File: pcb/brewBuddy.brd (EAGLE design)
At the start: 45.7 x 86.4 mm, 3 parts

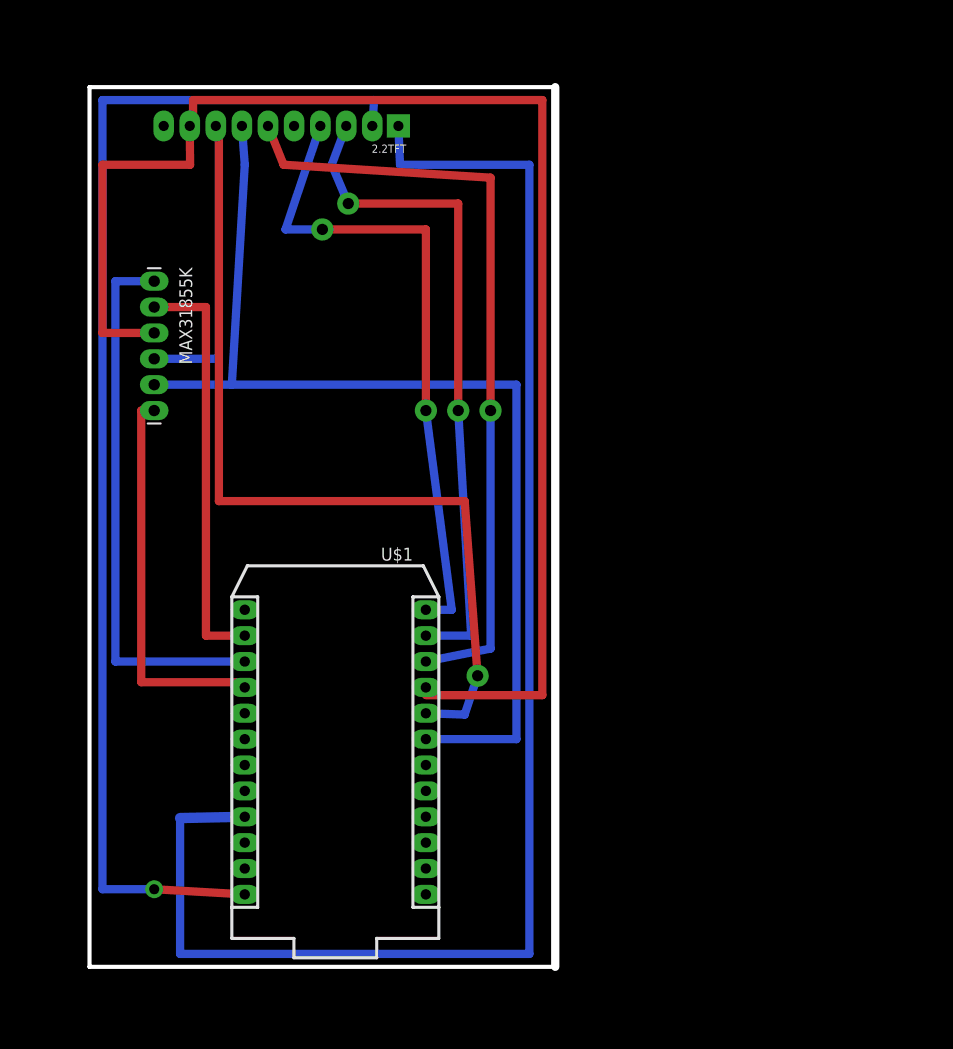
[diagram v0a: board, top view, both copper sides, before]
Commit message: updated brd for othermill
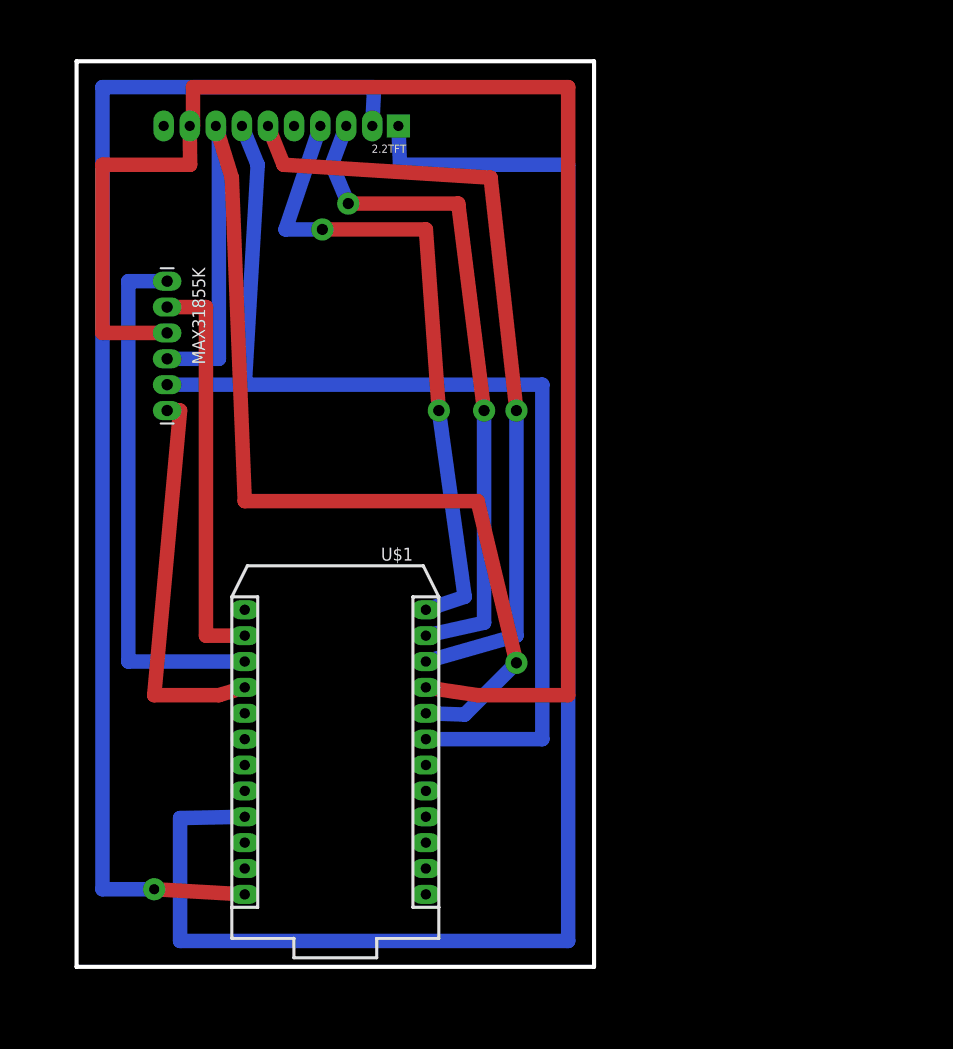
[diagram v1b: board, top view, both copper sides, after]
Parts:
- moved MAX31855K 1.27 mm to (7.62, 66.0)
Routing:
- net N$4: track 141.8 -> 150.0 mm
- net N$13: track 148.0 -> 153.0 mm
- net N$6: track 104.7 -> 108.8 mm
- net N$12: track 120.7 -> 123.2 mm
- net N$9: track 77.2 -> 78.8 mm
- net N$1: track 53.8 -> 52.6 mm
- net N$2: track 41.1 -> 39.9 mm
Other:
- board size 45.7 x 86.4 mm -> 50.8 x 88.9 mm

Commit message: moved traces to bottom layer for othermill
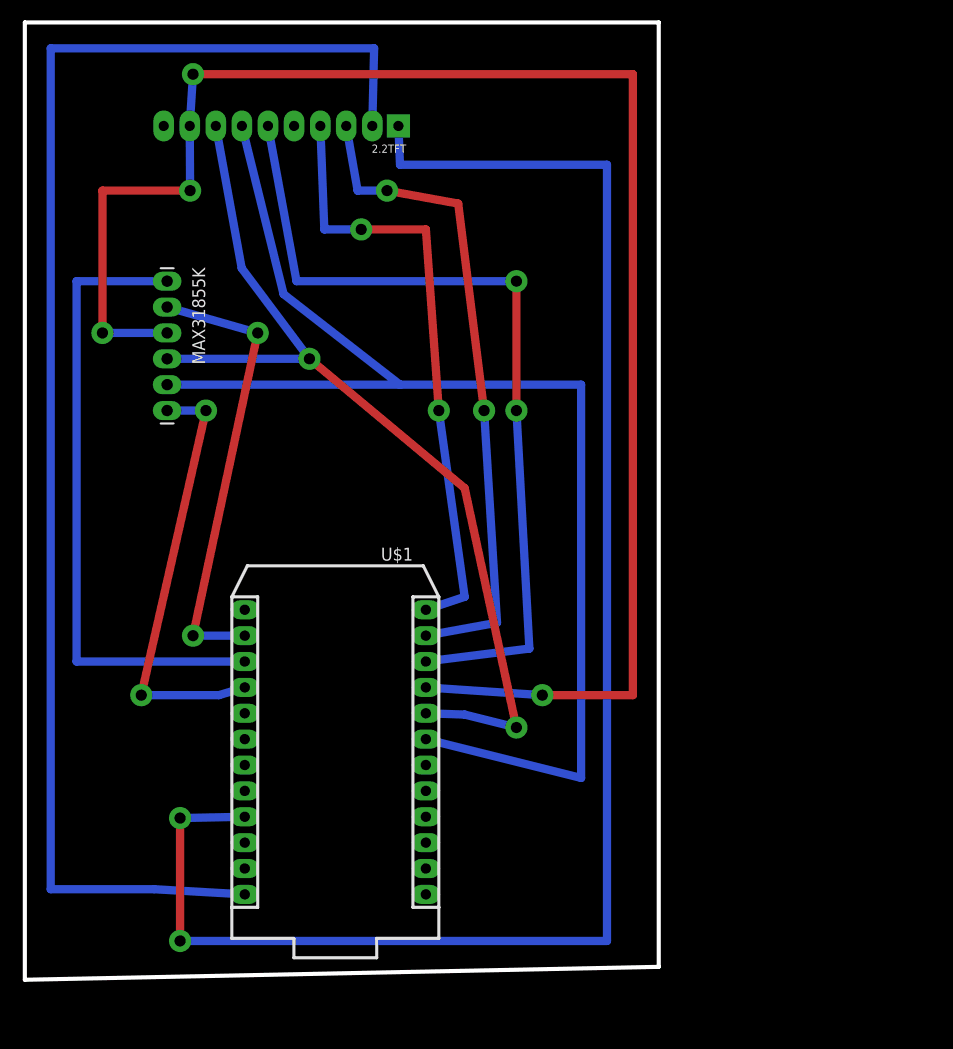
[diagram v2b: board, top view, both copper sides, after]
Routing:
- net N$5: track 115.5 -> 92.2 mm, vias 1 -> 2
- net N$12: track 123.2 -> 141.0 mm, vias 1 -> 0
- net N$6: track 108.8 -> 126.4 mm
- net N$4: track 150.0 -> 164.9 mm, vias 0 -> 4
- net N$1: track 52.6 -> 62.7 mm
- net N$13: track 153.0 -> 160.7 mm, vias 0 -> 2
- net N$2: track 39.9 -> 44.7 mm, vias 0 -> 2
- net N$9: track 78.8 -> 83.4 mm, vias 1 -> 2
- net N$3: track 38.3 -> 42.7 mm, vias 0 -> 2
- net N$10: track 64.8 -> 60.4 mm
- net N$11: track 66.2 -> 64.9 mm
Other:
- board size 50.8 x 88.9 mm -> 62.2 x 94 mm

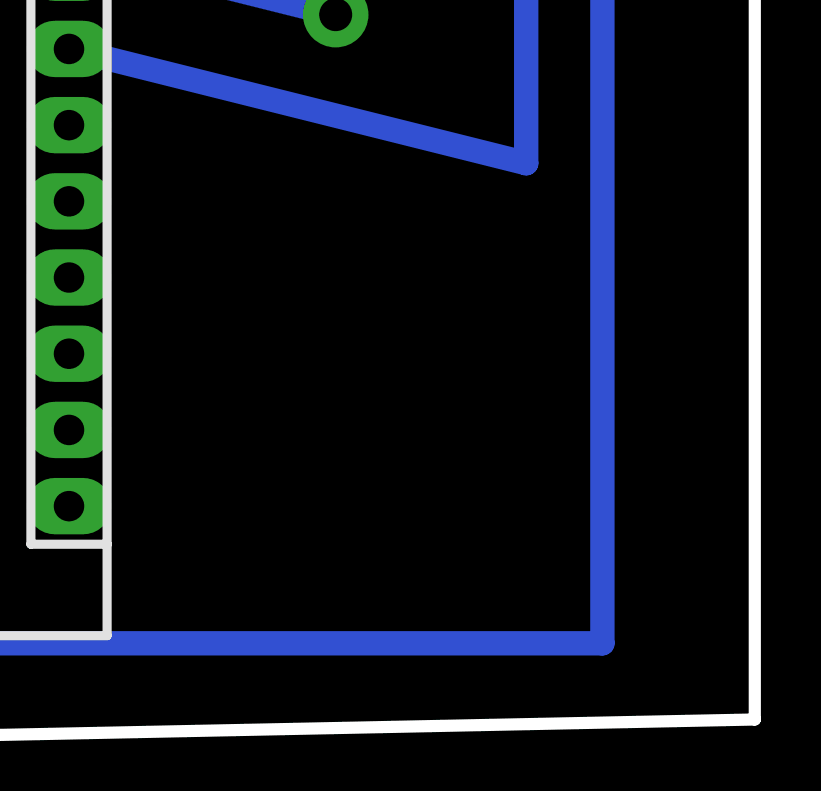
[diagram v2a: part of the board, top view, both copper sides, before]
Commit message: added BB name to board
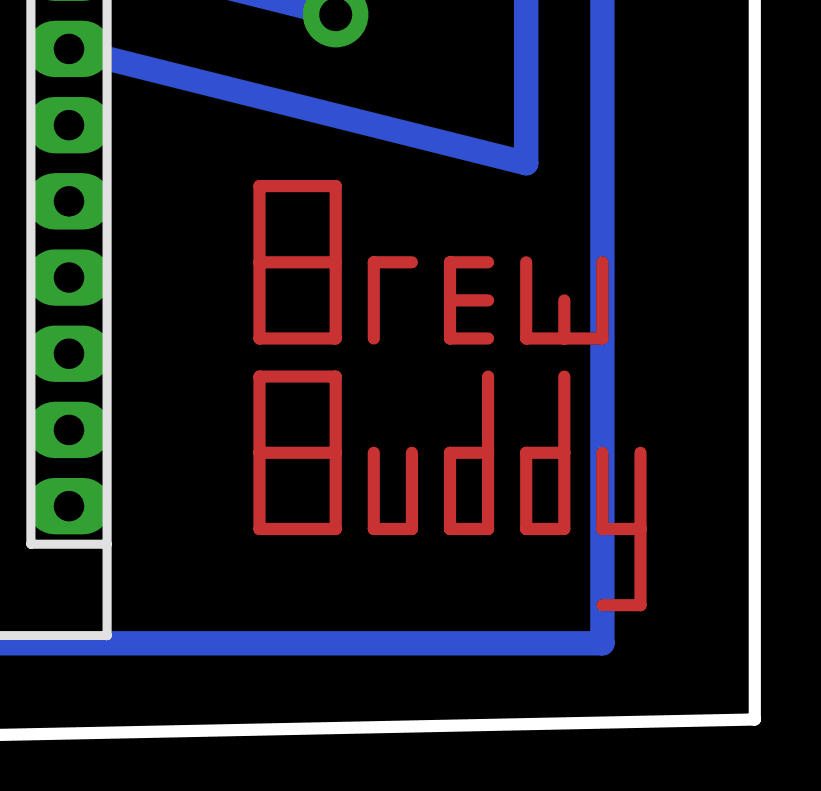
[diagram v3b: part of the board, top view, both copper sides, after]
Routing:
- net N$7: track 0.00 -> 17.8 mm
- net N$16: track 0.00 -> 17.8 mm
- net N$20: track 0.00 -> 10.2 mm
- net N$19: track 0.00 -> 10.2 mm
- net N$18: track 0.00 -> 10.2 mm
- net N$15: track 0.00 -> 8.89 mm
- net N$14: track 0.00 -> 6.35 mm
- net N$17: track 0.00 -> 6.35 mm
- net N$8: track 0.00 -> 3.81 mm
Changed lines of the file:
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@@
 <via x="11.43" y="53.34" extent="1-16" drill="1.1" diameter="2.1844"/>
+</signal>
+<signal name="N$7">
+<wire x1="39.37" y1="11.43" x2="39.37" y2="13.97" width="0.4064" layer="1"/>
+<wire x1="39.37" y1="13.97" x2="39.37" y2="16.51" width="0.4064" layer="1"/>
+<wire x1="39.37" y1="16.51" x2="41.91" y2="16.51" width="0.4064" layer="1"/>
+<wire x1="41.91" y1="16.51" x2="41.91" y2="13.97" width="0.4064" layer="1"/>
+<wire x1="39.37" y1="13.97" x2="41.91" y2="13.97" width="0.4064" layer="1"/>
+<wire x1="41.91" y1="13.97" x2="41.91" y2="11.43" width="0.4064" layer="1"/>
+<wire x1="41.91" y1="11.43" x2="39.37" y2="11.43" width="0.4064" layer="1"/>
+</signal>
+<signal name="N$8">
+<wire x1="43.18" y1="11.43" x2="43.18" y2="13.97" width="0.4064" layer="1"/>
+<wire x1="43.18" y1="13.97" x2="44.45" y2="13.97" width="0.4064" layer="1"/>
+</signal>
+<signal name="N$14">
+<wire x1="46.99" y1="11.43" x2="45.72" y2="11.43" width="0.4064" layer="1"/>
+<wire x1="45.72" y1="11.43" x2="45.72" y2="12.7" width="0.4064" layer="1"/>
+<wire x1="46.99" y1="12.7" x2="45.72" y2="12.7" width="0.4064" layer="1"/>
+<wire x1="45.72" y1="12.7" x2="45.72" y2="13.97" width="0.4064" layer="1"/>
+<wire x1="45.72" y1="13.97" x2="46.99" y2="13.97" width="0.4064" layer="1"/>
+</signal>
+<signal name="N$15">
+<wire x1="48.26" y1="13.97" x2="48.26" y2="11.43" width="0.4064" layer="1"/>
+<wire x1="48.26" y1="11.43" x2="49.53" y2="11.43" width="0.4064" layer="1"/>
+<wire x1="49.53" y1="12.7" x2="49.53" y2="11.43" width="0.4064" layer="1"/>
+<wire x1="49.53" y1="11.43" x2="50.8" y2="11.43" width="0.4064" layer="1"/>
+<wire x1="50.8" y1="11.43" x2="50.8" y2="13.97" width="0.4064" layer="1"/>
+</signal>
+<signal name="N$16">
+<wire x1="39.37" y1="5.08" x2="39.37" y2="7.62" width="0.4064" layer="1"/>
+<wire x1="39.37" y1="7.62" x2="39.37" y2="10.16" width="0.4064" layer="1"/>
+<wire x1="39.37" y1="10.16" x2="41.91" y2="10.16" width="0.4064" layer="1"/>
+<wire x1="41.91" y1="10.16" x2="41.91" y2="7.62" width="0.4064" layer="1"/>
+<wire x1="39.37" y1="7.62" x2="41.91" y2="7.62" width="0.4064" layer="1"/>
+<wire x1="41.91" y1="7.62" x2="41.91" y2="5.08" width="0.4064" layer="1"/>
+<wire x1="41.91" y1="5.08" x2="39.37" y2="5.08" width="0.4064" layer="1"/>
+</signal>
+<signal name="N$17">
+<wire x1="43.18" y1="7.62" x2="43.18" y2="5.08" width="0.4064" layer="1"/>
+<wire x1="43.18" y1="5.08" x2="44.45" y2="5.08" width="0.4064" layer="1"/>
+<wire x1="44.45" y1="5.08" x2="44.45" y2="7.62" width="0.4064" layer="1"/>
+</signal>
+<signal name="N$18">
+<wire x1="46.99" y1="7.62" x2="45.72" y2="7.62" width="0.4064" layer="1"/>
+<wire x1="45.72" y1="7.62" x2="45.72" y2="5.08" width="0.4064" layer="1"/>
+<wire x1="45.72" y1="5.08" x2="46.99" y2="5.08" width="0.4064" layer="1"/>
+<wire x1="46.99" y1="5.08" x2="46.99" y2="10.16" width="0.4064" layer="1"/>
+</signal>
+<signal name="N$19">
+<wire x1="49.53" y1="7.62" x2="49.53" y2="5.08" width="0.4064" layer="1"/>
+<wire x1="49.53" y1="5.08" x2="48.26" y2="5.08" width="0.4064" layer="1"/>
+<wire x1="48.26" y1="5.08" x2="48.26" y2="7.62" width="0.4064" layer="1"/>
+<wire x1="48.26" y1="7.62" x2="49.53" y2="7.62" width="0.4064" layer="1"/>
+<wire x1="49.53" y1="7.62" x2="49.53" y2="10.16" width="0.4064" layer="1"/>
+</signal>
+<signal name="N$20">
+<wire x1="50.8" y1="7.62" x2="50.8" y2="5.08" width="0.4064" layer="1"/>
+<wire x1="50.8" y1="5.08" x2="52.07" y2="5.08" width="0.4064" layer="1"/>
+<wire x1="52.07" y1="7.62" x2="52.07" y2="5.08" width="0.4064" layer="1"/>
+<wire x1="52.07" y1="5.08" x2="52.07" y2="2.54" width="0.4064" layer="1"/>
+<wire x1="52.07" y1="2.54" x2="50.8" y2="2.54" width="0.4064" layer="1"/>
 </signal>
 </signals>

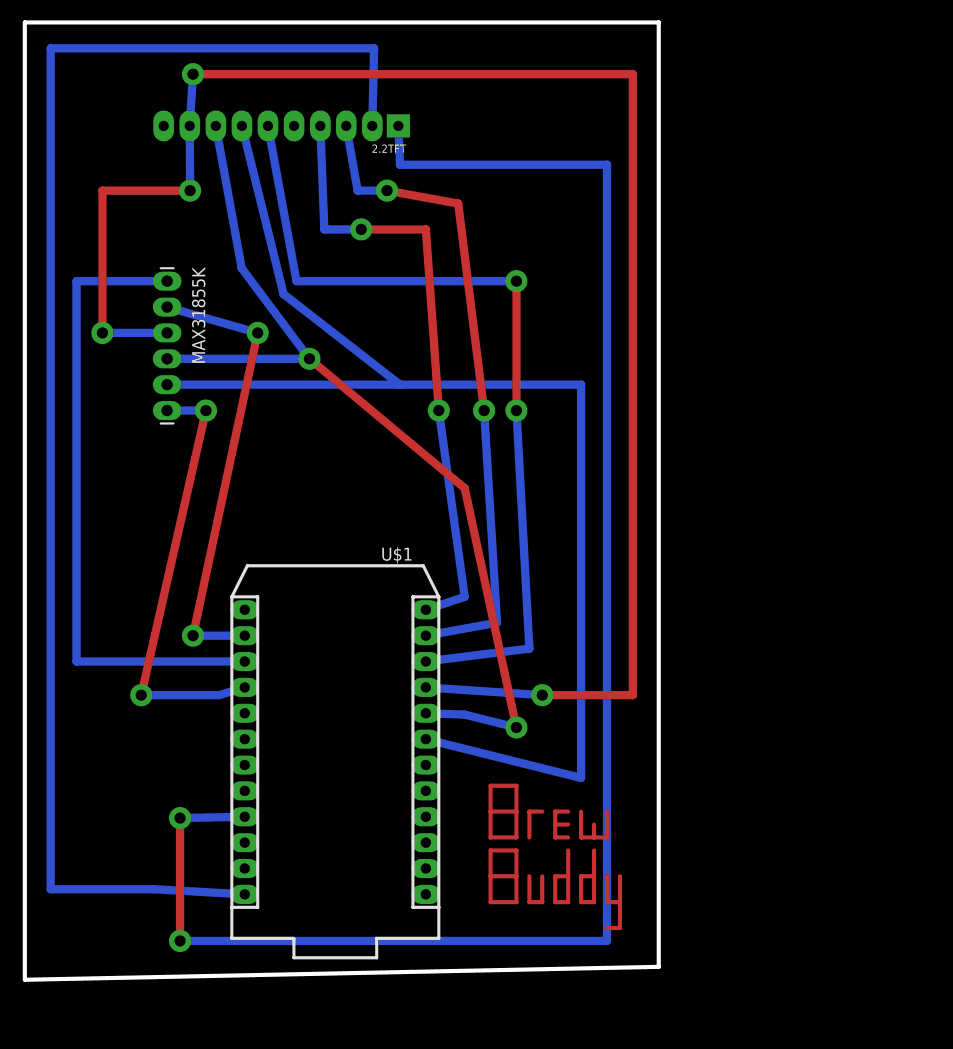
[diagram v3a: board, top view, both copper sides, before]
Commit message: modified BRD to make room for components
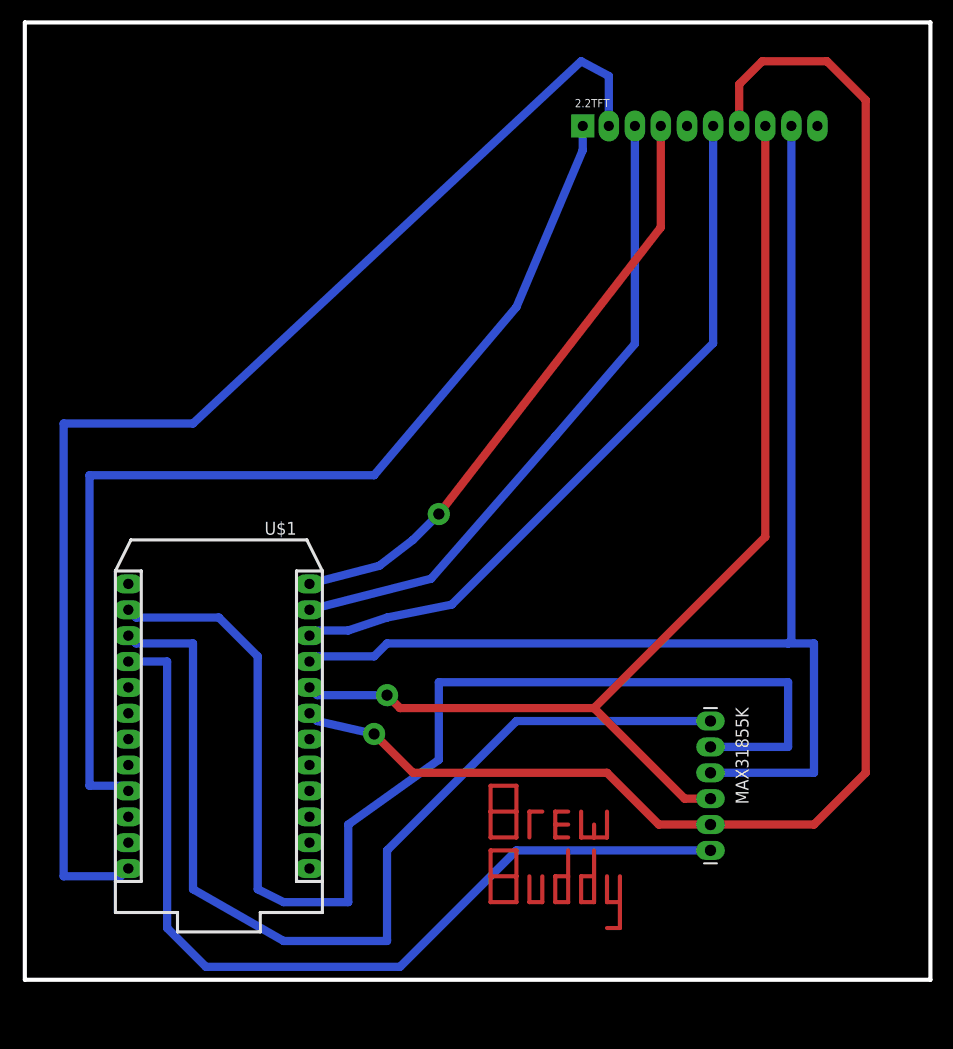
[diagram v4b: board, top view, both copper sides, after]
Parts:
- moved MAX31855K 68.6 mm to (61.0, 22.9)
- moved 2.2TFT 38.1 mm to (58.4, 81.3), turned to 0 degrees
- moved U$1 11.7 mm to (22.9, 40.6)
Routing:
- net N$2: track 44.7 -> 121.1 mm, vias 2 -> 0
- net N$13: track 160.7 -> 103.2 mm, vias 2 -> 0
- net N$3: track 42.7 -> 89.6 mm, vias 2 -> 0
- net N$4: track 164.9 -> 124.1 mm, vias 4 -> 0
- net N$1: track 62.7 -> 97.1 mm
- net N$6: track 126.4 -> 145.9 mm, vias 0 -> 1
- net N$12: track 141.0 -> 124.6 mm
- net N$5: track 92.2 -> 108.0 mm, vias 2 -> 1
- net N$9: track 83.4 -> 72.1 mm, vias 2 -> 0
- net N$11: track 64.9 -> 64.2 mm, vias 2 -> 0
- net N$10: vias 2 -> 1
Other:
- board size 62.2 x 94 mm -> 88.9 x 94 mm

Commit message: additional BRD mods
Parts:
- moved MAX31855K 10.9 mm to (54.6, 14.0)
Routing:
- net N$6: track 145.9 -> 175.7 mm, vias 1 -> 2
- net N$4: track 124.1 -> 139.3 mm
- net N$2: track 121.1 -> 136.3 mm
- net N$5: track 108.0 -> 122.0 mm, vias 1 -> 3
- net N$16: track 17.8 -> 30.5 mm
- net N$7: track 17.8 -> 30.5 mm
- net N$1: track 97.1 -> 85.8 mm
- net N$12: track 124.6 -> 135.0 mm
- net N$15: track 8.89 -> 16.5 mm
- net N$3: track 89.6 -> 84.1 mm
- net N$18: track 10.2 -> 15.2 mm
- net N$19: track 10.2 -> 15.2 mm
- net N$14: track 6.35 -> 11.4 mm
- net N$20: track 10.2 -> 15.2 mm
- net N$10: track 60.4 -> 64.5 mm, vias 1 -> 2
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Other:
- board size 88.9 x 94 mm -> 89 x 96.7 mm
